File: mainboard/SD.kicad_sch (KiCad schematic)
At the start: 2 parts, among them X1301 Micro SD-Card

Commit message: Layout complete
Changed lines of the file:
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@@
 		(exclude_from_sim no)
 		(at 12.7 12.7 0)
-		(size 271.78 13.97)
+		(size 271.78 20.32)
 		(margins 5.9999 5.9999 5.9999 5.9999)
 		(stroke
@@
 	(wire
 		(pts
+			(xy 102.87 66.04) (xy 102.87 85.09)
+		)
+		(stroke
+			(width 0)
+			(type default)
+		)
+	)
+	(wire
+		(pts
 			(xy 120.65 78.74) (xy 133.35 78.74)
 		)
@@
 		(pts
 			(xy 128.27 81.28) (xy 128.27 66.04)
-		)
-		(stroke
-			(width 0)
-			(type default)
-		)
-	)
-	(wire
-		(pts
-			(xy 102.87 83.82) (xy 102.87 85.09)
 		)
 		(stroke
@@
 	(symbol
 		(lib_id "power:+3V3")
-		(at 102.87 83.82 0)
+		(at 102.87 66.04 0)
 		(unit 1)
 		(exclude_from_sim no)
@@
 		(fields_autoplaced yes)
 		(property "Reference" "#PWR01301"
-			(at 102.87 87.63 0)
+			(at 102.87 69.85 0)
 			(effects
 				(font
@@
 		)
 		(property "Value" "+3V3"
-			(at 102.87 78.74 0)
+			(at 102.87 60.96 0)
 			(effects
 				(font
@@
 		)
 		(property "Footprint" ""
-			(at 102.87 83.82 0)
+			(at 102.87 66.04 0)
 			(effects
 				(font
@@
 		)
 		(property "Datasheet" ""
-			(at 102.87 83.82 0)
+			(at 102.87 66.04 0)
 			(effects
 				(font
@@
 		)
 		(property "Description" "Power symbol creates a global label with name \"+3V3\""
-			(at 102.87 83.82 0)
-			(effects
-				(font
+			(at 102.87 66.04 0)
+			(effects
+				(font

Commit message: Feature: Issue #10
- Replace SD card holder with MSD-4-A

Closes: #10

Signed-off-by: Daniel Kampert <DanielKampert@kampis-elektroecke.de>
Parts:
- X1301: footprint Connector_Card:microSD_HC_Hirose_DM3BT-DSF-PEJS -> Same Sky:MSD-4-A; manf Hirose Connector -> Same Sky; manf# DM3BT-DSF-PEJS -> MSD-4-A; mouser# 798-DM3BT-DSF-PEJS -> 179-MSD-4-A
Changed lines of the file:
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@@
 			)
 		)
-		(property "Footprint" "Connector_Card:microSD_HC_Hirose_DM3BT-DSF-PEJS"
+		(property "Footprint" "Same Sky:MSD-4-A"
 			(at 208.28 66.04 0)
 			(effects
@@
 			)
 		)
-		(property "Datasheet" "https://datasheet.lcsc.com/lcsc/2110151630_XKB-Connectivity-XKTF-015-N_C381082.pdf"
+		(property "Datasheet" "https://www.mouser.de/datasheet/3/6118/1/msd_4_a.pdf"
 			(at 156.21 81.28 0)
 			(effects
@@
 			)
 		)
-		(property "manf" "Hirose Connector"
+		(property "manf" "Same Sky"
+			(at 156.21 83.82 0)
+			(show_name yes)
+			(effects
+				(font
+					(size 1.27 1.27)
+					(italic yes)
+				)
+				(hide yes)
+			)
+		)
+		(property "manf#" "MSD-4-A"
 			(at 156.21 83.82 0)
 			(effects
@@
 			)
 		)
-		(property "manf#" "DM3BT-DSF-PEJS"
+		(property "mouser#" "179-MSD-4-A"
 			(at 156.21 83.82 0)
 			(effects
-				(font
-					(size 1.27 1.27)
-				)
-				(hide yes)
-			)
-		)
-		(property "mouser#" "798-DM3BT-DSF-PEJS"
-			(at 156.21 83.82 0)
-			(effects

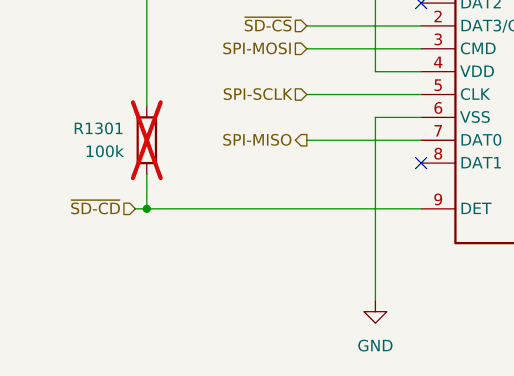
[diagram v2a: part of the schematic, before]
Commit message: Changed: Fix different minor assembly ToDos
Signed-off-by: Daniel Kampert <DanielKampert@kampis-elektroecke.de>
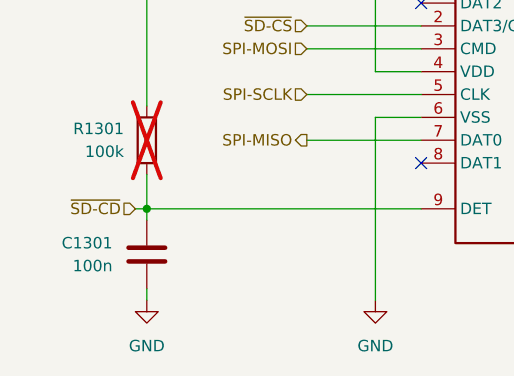
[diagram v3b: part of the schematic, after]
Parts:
- added C1301: 100n, Capacitor_SMD:C_0603_1608Metric, symbol Device:C
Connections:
- net GND: now also C1301.2
- net ~{SD-CD}: now also C1301.1
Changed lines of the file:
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@@
+	(wire
+		(pts
+			(xy 102.87 96.52) (xy 102.87 97.79)
+		)
+		(stroke
+			(width 0)
+			(type default)
+		)
+	)
 	(wire
 		(pts
 			(xy 133.35 96.52) (xy 102.87 96.52)
+		)
+		(stroke
+			(width 0)
+			(type default)
+		)
+	)
+	(wire
+		(pts
+			(xy 102.87 105.41) (xy 102.87 106.68)
 		)
 		(stroke
@@
 			)
 			(justify right)
+		)
+	)
+	(symbol
+		(lib_id "Device:C")
+		(at 102.87 101.6 0)
+		(unit 1)
+		(exclude_from_sim no)
+		(in_bom yes)
+		(on_board yes)
+		(dnp no)
+		(property "Reference" "C1301"
+			(at 99.06 100.3299 0)
+			(effects
+				(font
+					(size 1.27 1.27)
+				)
+				(justify right)
+			)
+		)
+		(property "Value" "100n"
+			(at 99.06 102.8699 0)
+			(effects
+				(font
+					(size 1.27 1.27)
+				)
+				(justify right)
+			)
+		)
+		(property "Footprint" "Capacitor_SMD:C_0603_1608Metric"
+			(at 103.8352 105.41 0)
+			(effects
+				(font
+					(size 1.27 1.27)
+				)
+				(hide yes)
+			)
+		)
+		(property "Datasheet" "https://www.mouser.de/datasheet/2/40/cx5r_KGM-3223198.pdf"
+			(at 102.87 101.6 0)
+			(effects
+				(font
+					(size 1.27 1.27)
+				)
+				(hide yes)
+			)
+		)
+		(property "Description" "Unpolarized capacitor"
+			(at 102.87 101.6 0)
+			(effects
+				(font
+					(size 1.27 1.27)
+				)
+				(hide yes)
+			)
+		)
+		(property "CONFIG" ""
+			(at 102.87 101.6 0)
+			(effects
+				(font
+					(size 1.27 1.27)
+				)
+				(hide yes)
+			)
+		)
+		(property "manf" "KYOCERA AVX"
+			(at 102.87 101.6 0)
+			(effects
+				(font
+					(size 1.27 1.27)
+				)
+				(hide yes)
+			)
+		)
+		(property "manf#" "06031C104MAT2A"
+			(at 102.87 101.6 0)
+			(effects
+				(font
+					(size 1.27 1.27)
+				)
+				(hide yes)
+			)
+		)
+		(property "mouser#" "581-06031C104MAT2A"
+			(at 102.87 101.6 0)
+			(effects
+				(font
+					(size 1.27 1.27)
+				)
+				(hide yes)
+			)
+		)
+		(pin "1"
+		)
+		(pin "2"
+		)
+		(instances
+			(project "Mainboard"
+				(path "/d5742f03-3b1a-42e5-a384-018bd4b919aa/c5103ceb-5325-4a84-a025-9638a412984e/9daf4182-cb00-4c79-b40e-4d55650908dc"
+					(reference "C1301")
+					(unit 1)
+				)
+			)
 		)
 	)
@@
 		(dnp no)
 		(fields_autoplaced yes)
-		(property "Reference" "#PWR01302"
+		(property "Reference" "#PWR01303"
 			(at 128.27 69.85 0)
 			(effects
@@
 			(project "PyroVision"
 				(path "/d5742f03-3b1a-42e5-a384-018bd4b919aa/c5103ceb-5325-4a84-a025-9638a412984e/9daf4182-cb00-4c79-b40e-4d55650908dc"
-					(reference "#PWR01302")
+					(reference "#PWR01303")
 					(unit 1)
 				)
@@
 		(dnp no)
 		(fields_autoplaced yes)
-		(property "Reference" "#PWR01304"
+		(property "Reference" "#PWR01305"
 			(at 177.8 113.03 0)
 			(effects
@@
 			(project "PyroVision"
 				(path "/d5742f03-3b1a-42e5-a384-018bd4b919aa/c5103ceb-5325-4a84-a025-9638a412984e/9daf4182-cb00-4c79-b40e-4d55650908dc"
-					(reference "#PWR01304")
+					(reference "#PWR01305")
 					(unit 1)
 				)
@@
 		(dnp no)
 		(fields_autoplaced yes)
-		(property "Reference" "#PWR01303"
+		(property "Reference" "#PWR01304"
 			(at 128.27 113.03 0)
 			(effects
@@
 			(project "PyroVision"
 				(path "/d5742f03-3b1a-42e5-a384-018bd4b919aa/c5103ceb-5325-4a84-a025-9638a412984e/9daf4182-cb00-4c79-b40e-4d55650908dc"
-					(reference "#PWR01303")
+					(reference "#PWR01304")
 					(unit 1)
 				)
@@
 					(unit 1)
 				)
+			)
+		)
+	)
+	(symbol
+		(lib_id "power:GND")
+		(at 102.87 106.68 0)
+		(unit 1)
+		(exclude_from_sim no)
+		(in_bom yes)
+		(on_board yes)
+		(dnp no)
+		(fields_autoplaced yes)
+		(property "Reference" "#PWR01302"
+			(at 102.87 113.03 0)
+			(effects
+				(font
+					(size 1.27 1.27)
+				)
+				(hide yes)
+			)
+		)
+		(property "Value" "GND"
+			(at 102.87 111.76 0)
+			(effects
+				(font
+					(size 1.27 1.27)
+				)
+			)
+		)
+		(property "Footprint" ""
+			(at 102.87 106.68 0)
+			(effects
+				(font
+					(size 1.27 1.27)
+				)
+				(hide yes)
+			)
+		)
+		(property "Datasheet" ""
+			(at 102.87 106.68 0)
+			(effects
+				(font
+					(size 1.27 1.27)
+				)
+				(hide yes)
+			)
+		)
+		(property "Description" "Power symbol creates a global label with name \"GND\" , ground"
+			(at 102.87 106.68 0)
+			(effects
+				(font
+					(size 1.27 1.27)
+				)
+				(hide yes)
+			)
+		)
+		(pin "1"
+		)
+		(instances
+			(project "Mainboard"
+				(path "/d5742f03-3b1a-42e5-a384-018bd4b919aa/c5103ceb-5325-4a84-a025-9638a412984e/9daf4182-cb00-4c79-b40e-4d55650908dc"
+					(reference "#PWR01302")
+					(unit 1)
+				)
